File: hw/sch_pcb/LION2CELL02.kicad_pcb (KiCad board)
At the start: 2 copper layers, 80.8 x 60.5 mm, 93 parts, among them J1 USBC_USB4105-GF-A, J10 HEADER_2x01_PARALLEL, J11 HEADER_1x02, J12 HEADER_2x05_PARALLEL, J2 CONN1_1, J3 CONN1_1, J4 JUMP_4X2, J5 USBC_USB4105-GF-A, J6 HEADER_2x01_PARALLEL, J7 HEADER_2x01_PARALLEL, J8 CONN1_1, J9 CONN1_1, Q1 DMT31M7LPS, Q2 AO3401A, Q3 DMT31M7LPS, Q5 DMT31M7LPS, SW1 SKRTLAE010, SW2 SKRTLAE010, U1 BQ25792RQMR1, U3 BQ40z50-R2

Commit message: Layout WiP.
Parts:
- removed J5: USBC_USB4105-GF-A, Mlab_CON:USBC GCT_USB4105-GF-A
- C12, C13, C14, C15, C16: footprint Capacitor_SMD:C_0603_1608Metric -> Capacitor_SMD:C_0805_2012Metric
- C17, C18, C2, C20, C9: footprint Capacitor_SMD:C_0402_1005Metric -> Capacitor_SMD:C_0805_2012Metric
- C21: footprint Capacitor_SMD:C_0402_1005Metric -> Capacitor_SMD:C_0805_2012Metric; moved to B.Cu
- C24: footprint Capacitor_SMD:C_0402_1005Metric -> Capacitor_SMD:C_0603_1608Metric; moved to B.Cu
- C25: footprint Capacitor_SMD:C_0603_1608Metric -> Capacitor_SMD:C_0805_2012Metric; moved to B.Cu
- C26, C27, C29, C30, C31, D6, FID1, FID2, FID3, FID4, J1, Q2, R17, TH3, TH4: moved to B.Cu
- C5: footprint Capacitor_SMD:C_0402_1005Metric -> Capacitor_SMD:C_0603_1608Metric
- Q1: footprint Mlab_IO:PowerDI5060-8 -> Mlab_T:D_POWERDI5060-8_6.0x5.1mm_P1.27mm
- Q3, Q5: footprint Mlab_IO:PowerDI5060-8 -> Mlab_T:D_POWERDI5060-8_6.0x5.1mm_P1.27mm; moved to B.Cu
- R11, R18, R19, R22, R23, R24, R27, R28, R3, R34, R36, R4, R5, R6, R9, TH1, TH2: footprint Resistor_SMD:R_0402_1005Metric -> Resistor_SMD:R_0805_2012Metric
- R35: value 1mR -> 2mR; footprint Resistor_SMD:R_1206_3216Metric -> Resistor_SMD:R_2512_6332Metric
- moved H2 102.8 mm to (184.1, 79.6)
- moved Q3 94.4 mm to (193.5, 101.4), turned to 90 degrees
- moved H4 85.0 mm to (184.1, 130.4)
- moved R7 70.2 mm to (142.8, 149.2)
- moved D3 69.8 mm to (142.9, 144.6)
- moved D1 62.8 mm to (151.7, 131.5), turned to -90 degrees
- moved Q5 61.9 mm to (160.2, 93.6), turned to 180 degrees
- moved TH2 60.9 mm to (176.3, 95.4)
- moved J4 60.6 mm to (173.4, 130.0), turned to -90 degrees
- moved D4 60.0 mm to (154.7, 131.5)
- moved D5 59.2 mm to (157.9, 131.5)
- moved H1 57.6 mm to (112.9, 79.6)
- moved TH1 52.1 mm to (176.3, 114.7), turned to 180 degrees
- moved C31 51.9 mm to (137.3, 99.7)
- moved R32 47.6 mm to (116.4, 95.5), turned to 0 degrees
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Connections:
- net /Fuel Gauge/PS+ renamed /Fuel Gauge/SR+
- net /Fuel Gauge/PS- renamed /Fuel Gauge/SR-
- net /Power Input/PMID renamed Net-(U1-PMID)
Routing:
- net GND: track 646.2 -> 0.00 mm, vias 202 -> 0
- net (no net): track 135.9 -> 0.00 mm, vias 7 -> 0
- net /BAT+: track 100.7 -> 0.00 mm, vias 1 -> 0
- net +3V3: track 96.3 -> 0.00 mm, vias 4 -> 0
- net Net-(C10-Pad1): track 70.9 -> 0.00 mm, vias 2 -> 0
- net Net-(D1-K): track 65.7 -> 0.00 mm, vias 2 -> 0
- net Net-(D1-A): track 58.6 -> 0.00 mm, vias 21 -> 0
- net Net-(D3-A): track 37.4 -> 0.00 mm, vias 2 -> 0
- net /SDA: track 35.8 -> 0.00 mm
- net /SCL: track 34.9 -> 0.00 mm
- net /HDQ: track 34.6 -> 0.00 mm
- net Net-(SW1-Pad2): track 31.4 -> 0.00 mm
- net /CMODE: track 31.3 -> 0.00 mm, vias 1 -> 0
- net /CE: track 31.0 -> 0.00 mm, vias 1 -> 0
- net Net-(C14-Pad1): track 28.1 -> 0.00 mm, vias 2 -> 0
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- removed copper zone on B.Cu, net (none)
- removed copper zone on B.Cu, net /Fuel Gauge/PACK+
- removed copper zone on B.Cu, net /Power Input/REGN
- removed copper zone on B.Cu, net Net-(Q3-G)
- removed copper zone on B.Cu, net Net-(U1-BATP)
- removed copper zone on B.Cu, net Net-(U1-SW1)
- removed copper zone on B.Cu, net Net-(U1-SW2)
- removed copper zone on B.Cu, net VBUS
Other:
- board text added: "2024"
- board text added: "LION2CELL02A"
- board text added: "kaklik"
- board text removed: "2016"
- board text removed: "3"
- board text removed: "4"
- board text removed: "5"
- board text removed: "6"
- board text removed: "HDQ"
- board text removed: "JACHO"
- board text removed: "LION2CELL01D"

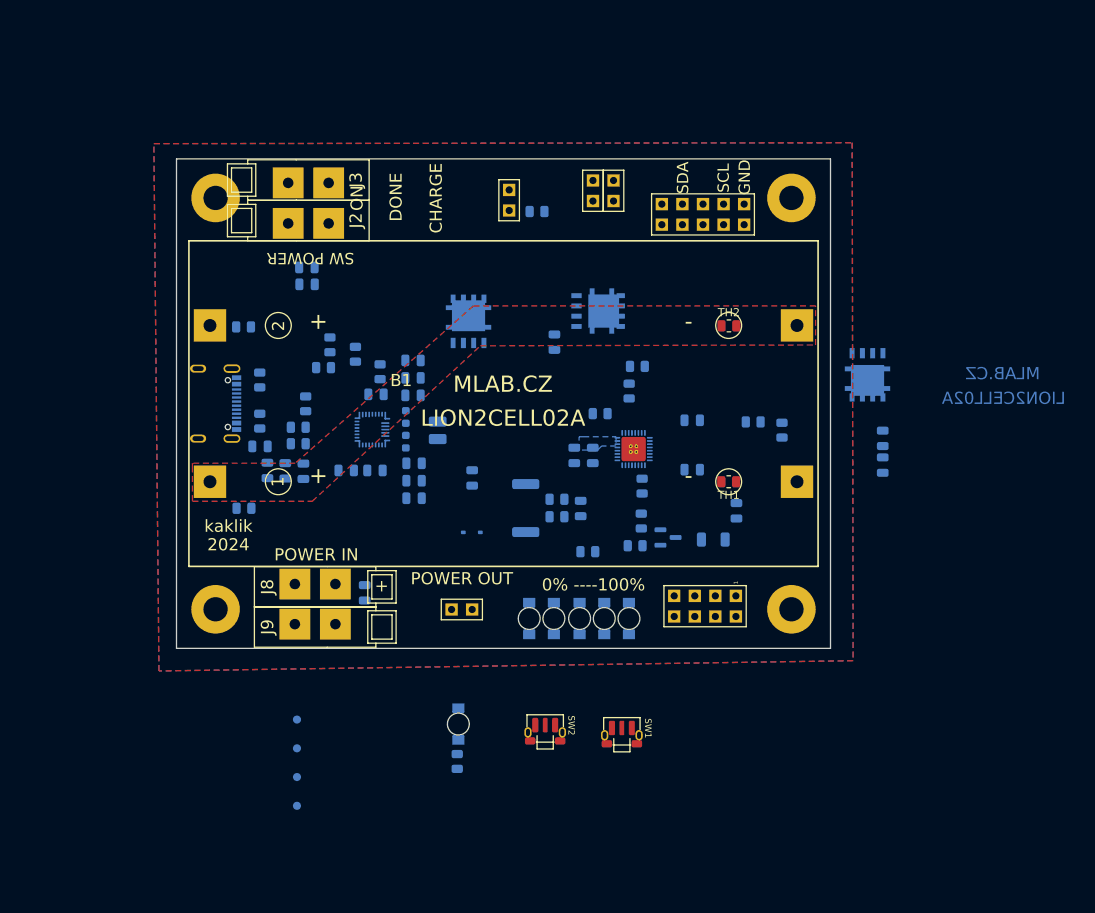
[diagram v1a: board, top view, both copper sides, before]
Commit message: Partially routed PCB.
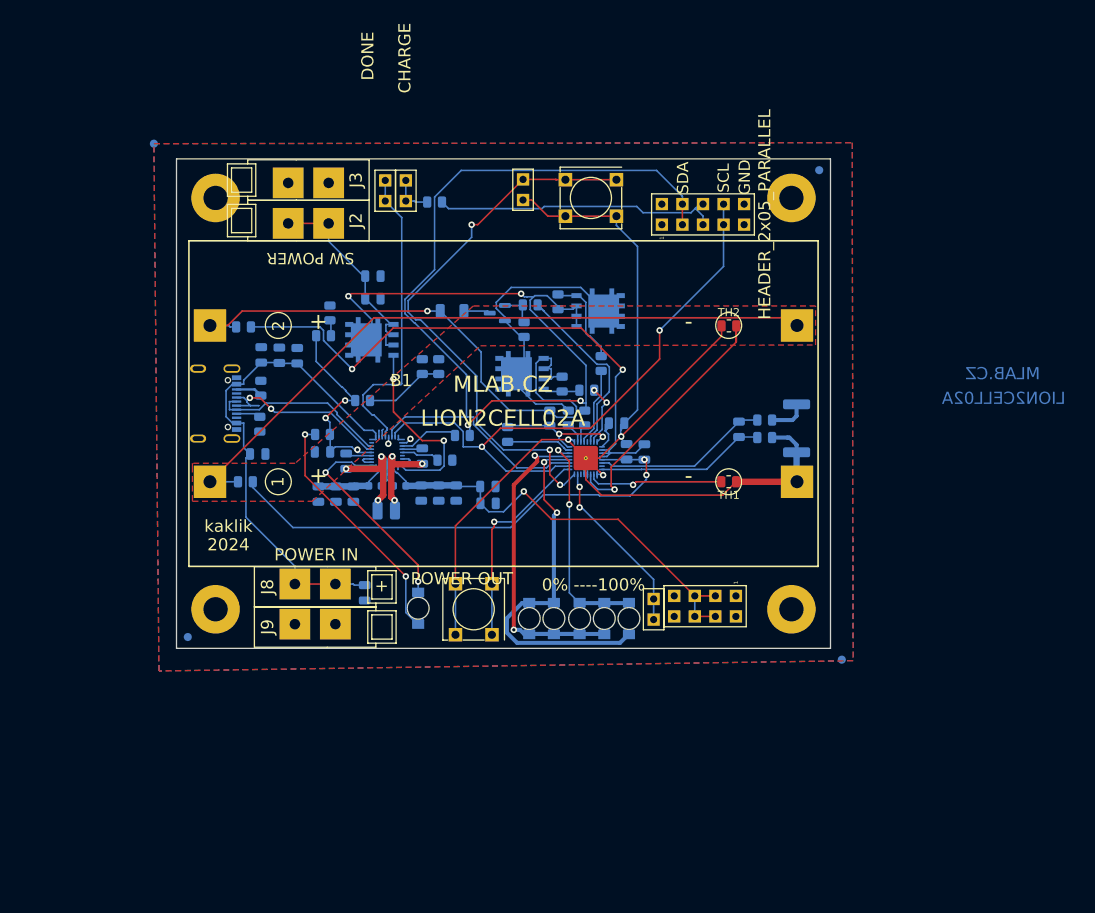
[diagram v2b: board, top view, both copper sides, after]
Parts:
- removed C12, C13, C14, C15: 100nF, Capacitor_SMD:C_0805_2012Metric
- D6: footprint Diode_SMD:D_SOD-323 -> Diode_SMD:D_0805_2012Metric
- SW1, SW2: value SKRTLAE010 -> SW_Push; footprint Mlab_SW:SKRT -> Mlab_SW:SW_PUSH_SMALL
- moved FID2 96.2 mm to (187.5, 76.2)
- moved FID4 83.7 mm to (105.3, 72.9)
- moved FID3 68.8 mm to (190.3, 136.6)
- moved SW1 65.6 mm to (159.3, 79.6)
- moved J7 52.6 mm to (133.9, 78.7), turned to 180 degrees
- moved J10 52.2 mm to (167.0, 130.4)
- moved R7 43.7 mm to (126.1, 108.8), turned to 180 degrees
- moved R17 42.9 mm to (142.2, 93.6), turned to 0 degrees
- moved Q3 42.7 mm to (150.8, 101.3), turned to 0 degrees
- moved C7 35.1 mm to (146.6, 115.2)
- moved C8 35.1 mm to (146.6, 117.3)
- moved R35 34.9 mm to (184.7, 108.0), turned to 90 degrees
- moved Q2 34.8 mm to (147.7, 93.8), turned to 180 degrees
- moved R19 32.4 mm to (151.8, 92.8), turned to 180 degrees
- moved R36 28.3 mm to (180.8, 107.0), turned to 180 degrees
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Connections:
- J12 pad 3: Net-(J12-Pad3) -> /Fuel Gauge/SCL
- J12 pad 4: Net-(J12-Pad3) -> /Fuel Gauge/SCL
- J12 pad 7: Net-(J12-Pad7) -> /Fuel Gauge/SDA
- J12 pad 8: Net-(J12-Pad7) -> /Fuel Gauge/SDA
- U1 pad 14: /Power Input/SCL -> /Fuel Gauge/SCL
- U1 pad 15: /Power Input/SDA -> /Fuel Gauge/SDA
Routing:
- net GND1: track 0.00 -> 153.7 mm, vias 0 -> 3
- net /Fuel Gauge/SCL: track 0.00 -> 95.5 mm
- net Net-(B1A--): track 0.00 -> 84.7 mm
- net /Fuel Gauge/B+: track 0.00 -> 75.8 mm, vias 0 -> 1
- net /Fuel Gauge/SDA: track 0.00 -> 75.2 mm, vias 0 -> 2
- net /Fuel Gauge/PACK+: track 0.00 -> 73.3 mm, vias 0 -> 4
- net Net-(U3-VC2): track 0.00 -> 71.9 mm, vias 0 -> 2
- net Net-(U3-~{PRES/SHDWN}): track 0.00 -> 69.4 mm, vias 0 -> 3
- net VBUS: track 0.00 -> 64.1 mm
- net Net-(U3-VC1): track 0.00 -> 61.8 mm, vias 0 -> 2
- net /Power Input/System_load: track 0.00 -> 55.5 mm, vias 0 -> 1
- net Net-(D1-A): track 0.00 -> 45.9 mm, vias 0 -> 2
- net Net-(D1-K): track 0.00 -> 44.8 mm, vias 0 -> 2
- net Net-(U1-nQON): track 0.00 -> 38.0 mm
- net +3.3V: track 0.00 -> 35.9 mm
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- removed copper zone on B.Cu, net /Fuel Gauge/SR-
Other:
- board text removed: "ON"

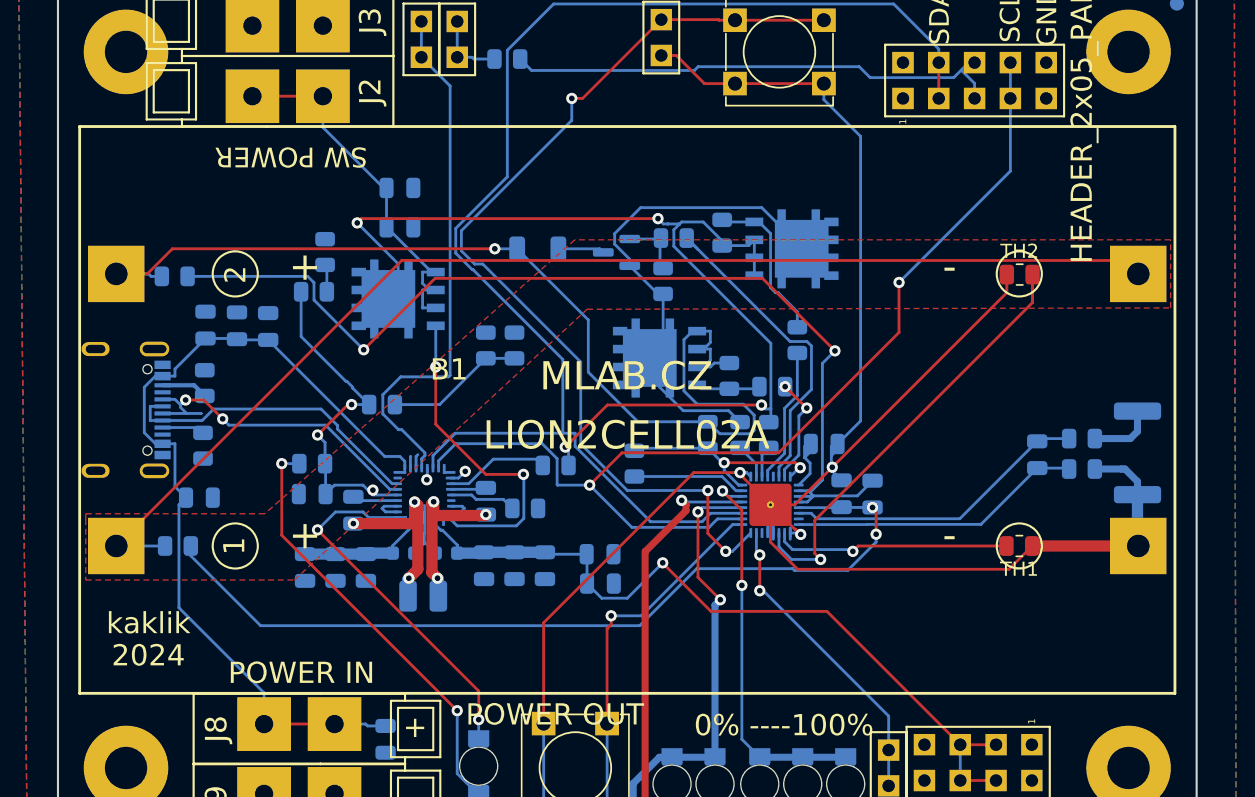
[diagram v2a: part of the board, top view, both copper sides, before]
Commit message: Routed few aditional nets Battery mid-point zone connection changed to a track with special net class.
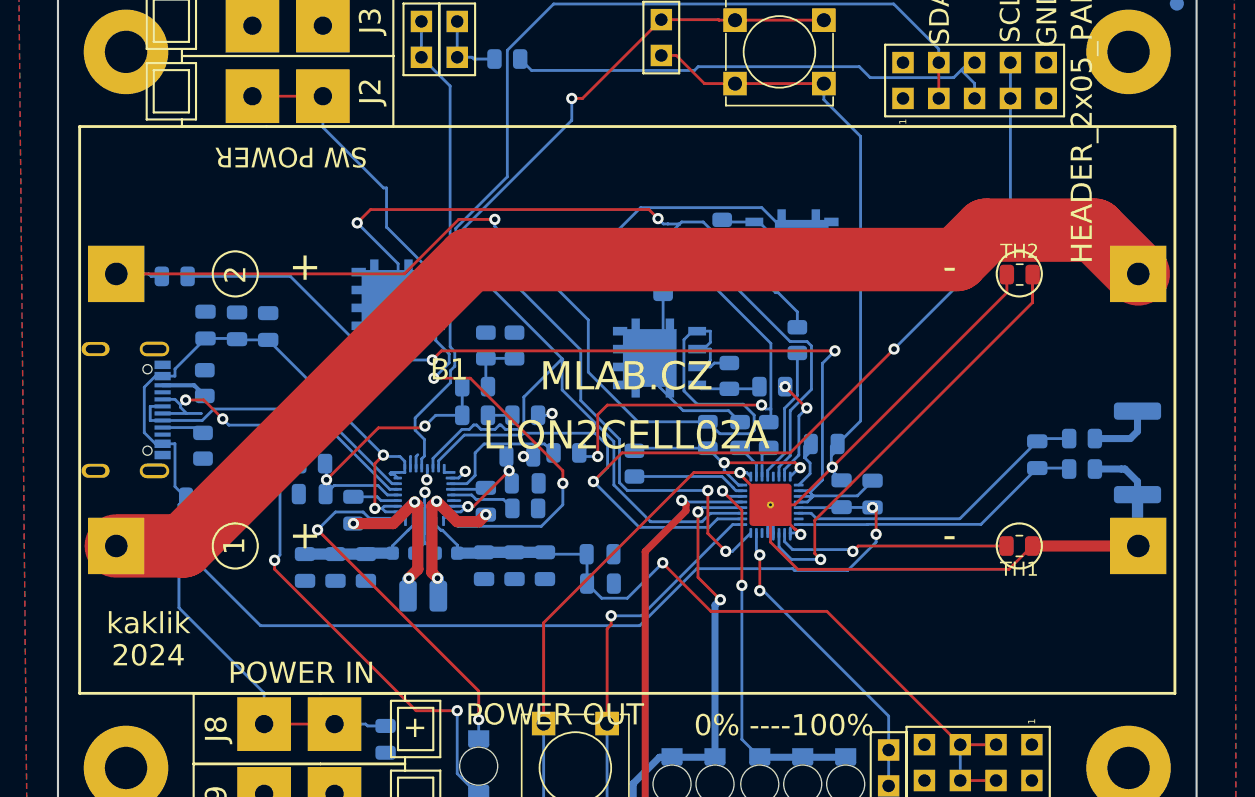
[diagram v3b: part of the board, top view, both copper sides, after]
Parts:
- moved C11 20.9 mm to (140.9, 108.3)
- moved C19 20.2 mm to (141.3, 110.2)
- moved R4 18.3 mm to (141.3, 105.4), turned to 0 degrees
- moved R3 14.4 mm to (137.7, 105.4)
- moved R5 6.73 mm to (137.7, 103.3)
- moved R8 1.17 mm to (144.2, 108.0)
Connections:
- net Net-(B1A--) renamed /Fuel Gauge/BAT_MID
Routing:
- net /Power Input/Power_load: track 28.4 -> 34.7 mm, vias 0 -> 2
- net VBUS: track 64.1 -> 70.0 mm, vias 0 -> 2
- net Net-(U1-TS): track 9.84 -> 4.10 mm
- net Net-(U3-VC2): track 71.9 -> 67.5 mm
- net Net-(Q1-G): track 23.6 -> 27.8 mm
- net Net-(U1-nQON): track 38.0 -> 34.2 mm
- net /Power Input/REGN: track 25.0 -> 21.4 mm, vias 3 -> 2
- net /Fuel Gauge/SCL: track 95.5 -> 98.8 mm
- net /Fuel Gauge/BAT_MID: track 84.7 -> 87.9 mm
- net GND: track 12.1 -> 14.9 mm, vias 1 -> 4
- net /Fuel Gauge/SDA: track 75.2 -> 77.8 mm
- net Net-(U1-BATP): track 7.42 -> 9.65 mm
- net /Fuel Gauge/B+: track 75.8 -> 77.8 mm
- net Net-(D3-A): track 30.5 -> 32.2 mm
- net Net-(U1-SW1): track 14.2 -> 13.3 mm
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- removed copper zone on F.Cu, net /Power Input/REGN

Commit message: PCB routing WiP.
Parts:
- moved J11 78.7 mm to (167.3, 155.5)
- moved R11 75.0 mm to (153.5, 153.9)
- moved J6 75.0 mm to (149.9, 152.5)
- moved J7 75.0 mm to (147.4, 152.5)
- moved R22 39.4 mm to (119.5, 87.1), turned to -90 degrees
- moved R28 36.4 mm to (123.4, 94.8), turned to 90 degrees
- moved Q3 29.3 mm to (124.5, 88.5), turned to 180 degrees
- moved Q5 28.8 mm to (131.9, 88.5), turned to 0 degrees
- moved J4 26.8 mm to (146.6, 129.0)
- moved J10 25.2 mm to (165.3, 155.5)
- moved R18 24.4 mm to (126.9, 92.6), turned to 180 degrees
- moved R17 22.7 mm to (119.5, 91.2), turned to -90 degrees
- moved R19 21.0 mm to (130.8, 94.7)
- moved Q2 20.9 mm to (126.9, 95.5)
- moved R23 18.4 mm to (136.9, 90.1), turned to 90 degrees
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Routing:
- net /Fuel Gauge/PACK+: track 73.5 -> 28.7 mm, vias 4 -> 0
- net Net-(U3-CHG): track 7.68 -> 48.0 mm
- net Net-(U1-nQON): track 34.2 -> 0.00 mm
- net +3.3V: track 35.9 -> 2.54 mm
- net Net-(Q1-G): track 27.8 -> 0.00 mm, vias 2 -> 0
- net /Fuel Gauge/VCOM: track 35.0 -> 7.37 mm
- net /Fuel Gauge/SCL: track 98.8 -> 71.7 mm, vias 0 -> 3
- net /Power Input/System_load: track 55.5 -> 32.0 mm, vias 1 -> 0
- net Net-(U3-BTP_INT): track 22.0 -> 0.00 mm, vias 2 -> 0
- net Net-(U3-PCHG): track 23.4 -> 42.0 mm, vias 0 -> 2
- net Net-(U3-DSG): track 9.64 -> 24.1 mm, vias 0 -> 2
- net /Power Input/Power_load: track 34.7 -> 20.6 mm, vias 2 -> 0
- net Net-(D1-A): track 45.9 -> 59.5 mm
- net Net-(U3-PACK): track 2.24 -> 15.3 mm
- net Net-(Q3-G): track 4.70 -> 13.9 mm, vias 0 -> 2
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
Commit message: Routed another tracks.
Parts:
- Q2: value AO3401A -> AP2305AGN-HF-3
- moved J10 77.8 mm to (148.5, 79.6)
- moved J11 77.8 mm to (150.5, 79.6)
- moved J6 73.1 mm to (146.0, 79.5)
- moved J7 73.1 mm to (143.4, 79.5)
- moved R11 70.8 mm to (146.7, 83.4)
- moved C3 12.1 mm to (130.7, 106.0)
- moved C2 11.9 mm to (132.8, 106.0)
- moved R7 3.94 mm to (126.1, 112.7)
- moved R24 1.91 mm to (146.6, 103.3)
- moved R27 1.81 mm to (143.0, 97.4), turned to 0 degrees
- moved R8 1.08 mm to (144.7, 105.4), turned to 0 degrees
- moved C20 0.25 mm to (126.1, 110.7)
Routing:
- net /Fuel Gauge/VCOM: track 7.37 -> 61.0 mm, vias 0 -> 2
- net /Power Input/Power_load: track 20.6 -> 60.0 mm
- net Net-(Q1-G): track 0.00 -> 38.2 mm, vias 0 -> 2
- net Net-(U3-BTP_INT): track 0.00 -> 29.7 mm
- net /Fuel Gauge/PACK+: track 28.7 -> 46.7 mm
- net Net-(U1-TS): track 4.89 -> 13.5 mm, vias 0 -> 2
- net Net-(Q2-D): track 0.00 -> 7.61 mm
- net VBUS: track 69.7 -> 76.9 mm
- net GND: track 12.1 -> 17.4 mm, vias 2 -> 5
- net Net-(U3-VC1): track 65.7 -> 60.7 mm
- net Net-(D3-A): track 30.2 -> 26.0 mm
- net Net-(Q2-G): track 0.00 -> 3.84 mm
- net /Fuel Gauge/SDA: track 74.9 -> 71.1 mm, vias 2 -> 3
- net Net-(U3-DSG): track 24.1 -> 26.9 mm
- net Net-(U3-~{PRES/SHDWN}): track 62.4 -> 59.9 mm
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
